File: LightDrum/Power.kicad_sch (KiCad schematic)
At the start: 67 parts, among them U1001 AP3401, U1002 LM22673-SOIC, U701 INA4181 A2, U702 INA4181 A2, U901 74HC2G08

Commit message: Lock REV8 Layout and send to PCB MNF
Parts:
- removed C1021: 100nF, Capacitor_SMD:C_0603_1608Metric, symbol Device:C_Small
- removed U901: 74HC2G08, Package_SO:TSSOP-8_3x3mm_P0.65mm, symbol Daxxn_Logic:74HCT2G08
- renumbered U-XLR-VREF1001 to U1003
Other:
- note removed: "PS LOCKOUT"
- moved on the sheet: C1005, C1022, C1023, C1024, C1025, C1042, C1043, L1002, L1004, R1008, R1009, R1010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

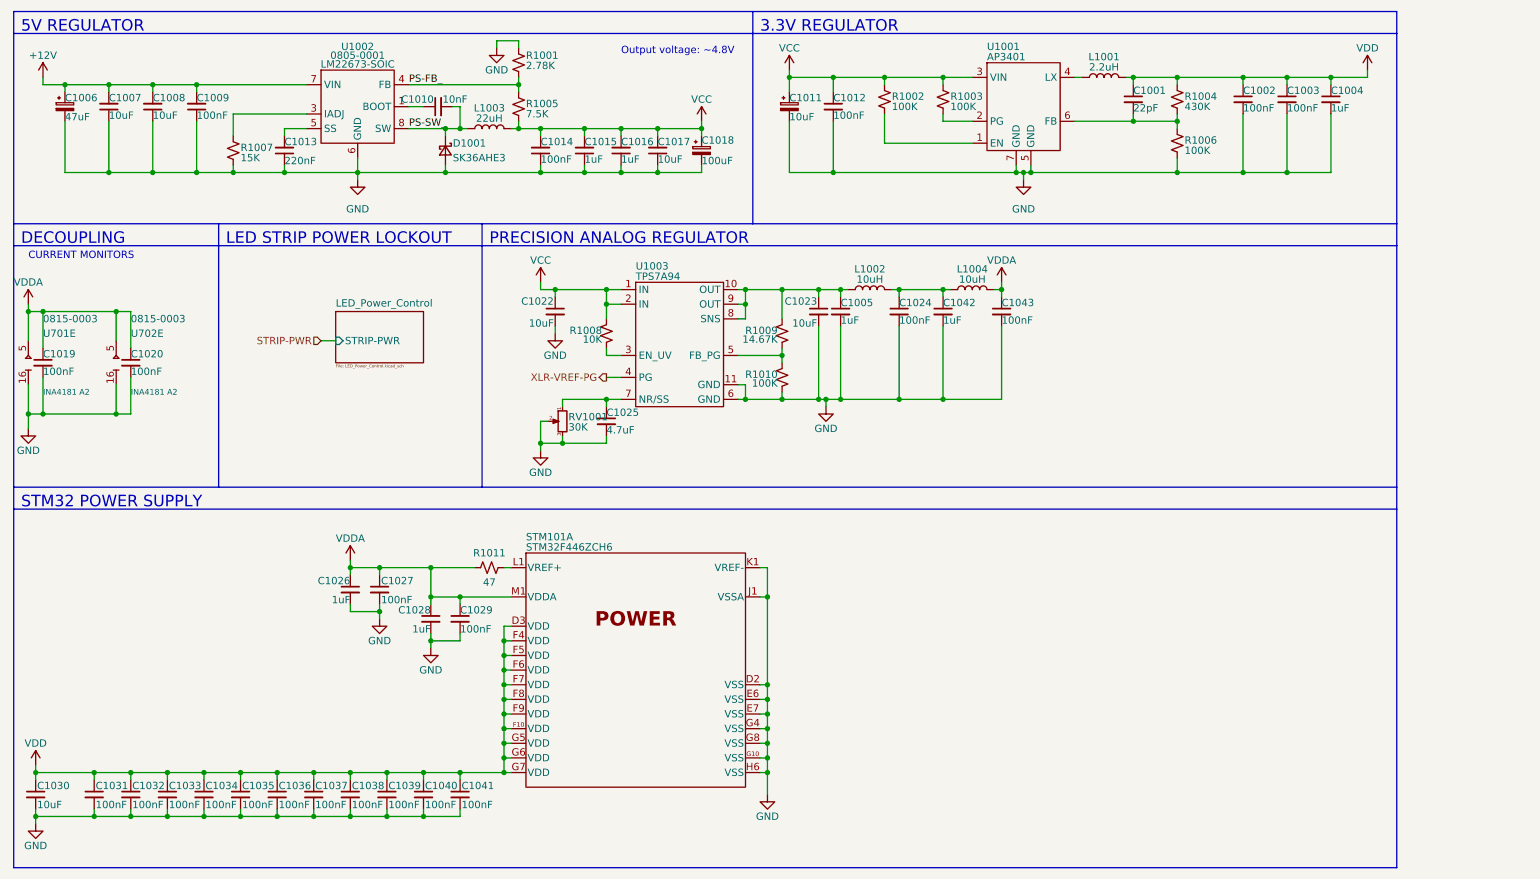
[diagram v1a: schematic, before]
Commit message: Replace old MCU W/ STM32F412
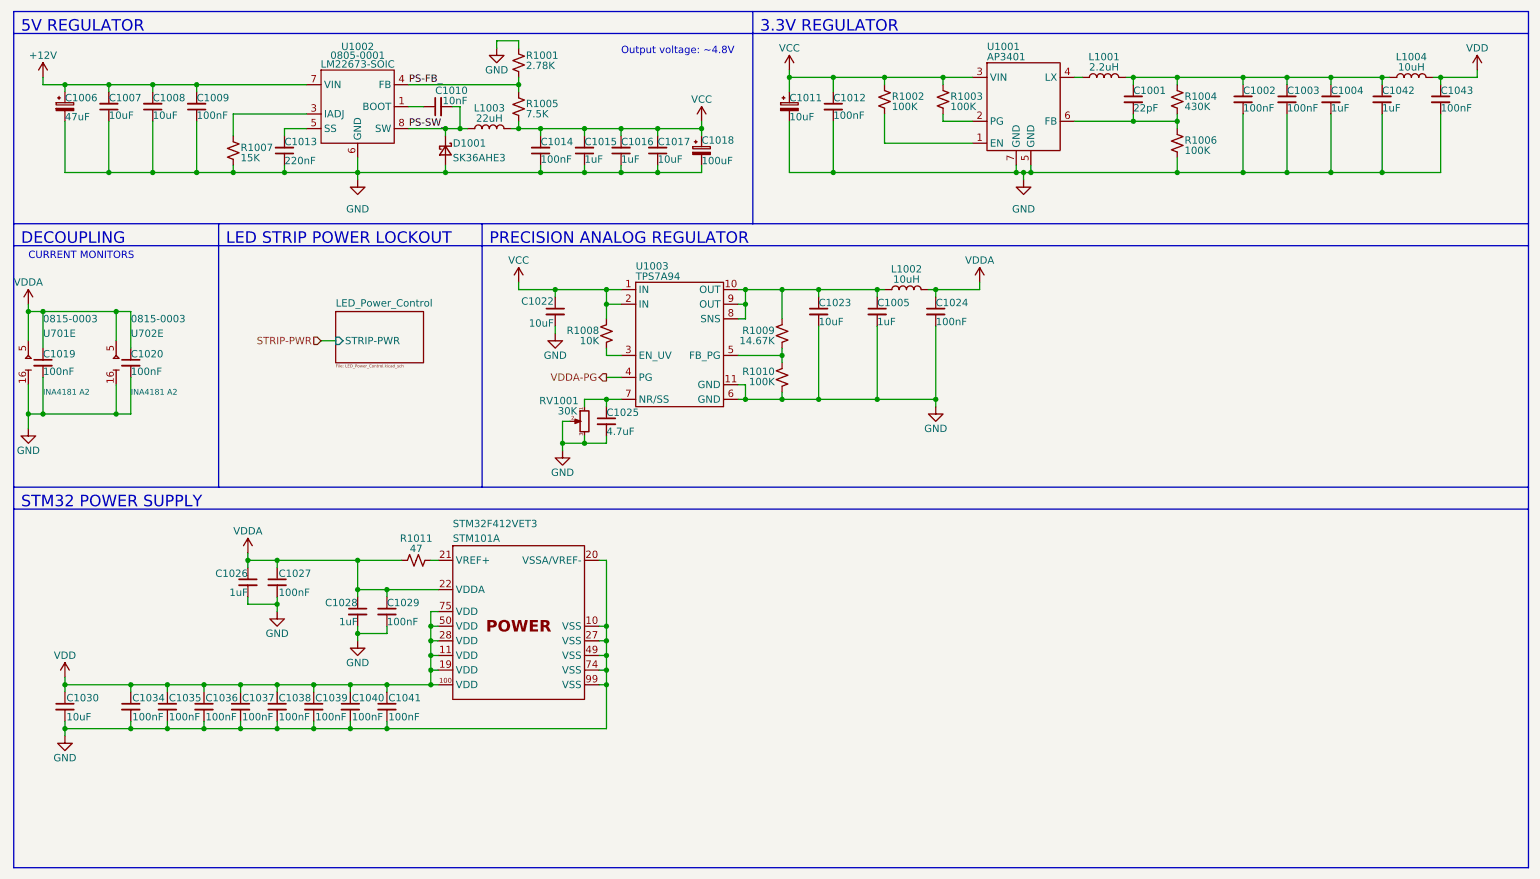
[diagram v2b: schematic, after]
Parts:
- removed C1031, C1032, C1033: 100nF, Capacitor_SMD:C_0402_1005Metric, symbol Device:C_Small
- removed STM101: STM32F446ZCH6, Daxxn_Packages:UFBGA144-7x7xOP6, symbol Daxxn_STMicros:STM32F446ZCH6
- added STM101: STM32F412VET3, Package_QFP:LQFP-100_14x14mm_P0.5mm, symbol Daxxn_STMicros:STM32F412VET3
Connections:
- net GND: now also STM101.10 (VSS), STM101.20 (VSSA/VREF-), STM101.27 (VSS), STM101.49 (VSS), STM101.74 (VSS), STM101.99 (VSS)
- net VDD: now also C1043.1, L1004.2, STM101.100 (VDD), STM101.11 (VDD), STM101.19 (VDD), STM101.28 (VDD), STM101.50 (VDD), STM101.75 (VDD); no longer C1001.1, C1002.1, C1003.1, C1004.1, L1001.2, R1004.1
- net VDDA: now also C1024.1, L1002.2, STM101.22 (VDDA); no longer C1043.1, L1004.2
- net at R1011.1: now also STM101.21 (VREF+)
- net at C1042.1, L1004.1: now also C1001.1, C1002.1, C1003.1, C1004.1, L1001.2, R1004.1; no longer C1024.1, L1002.2
- net XLR-VREF-PG renamed VDDA-PG
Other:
- moved on the sheet: C1005, C1024, C1026, C1027, C1028, C1029, C1030, C1034, C1035, C1036, C1037, C1038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

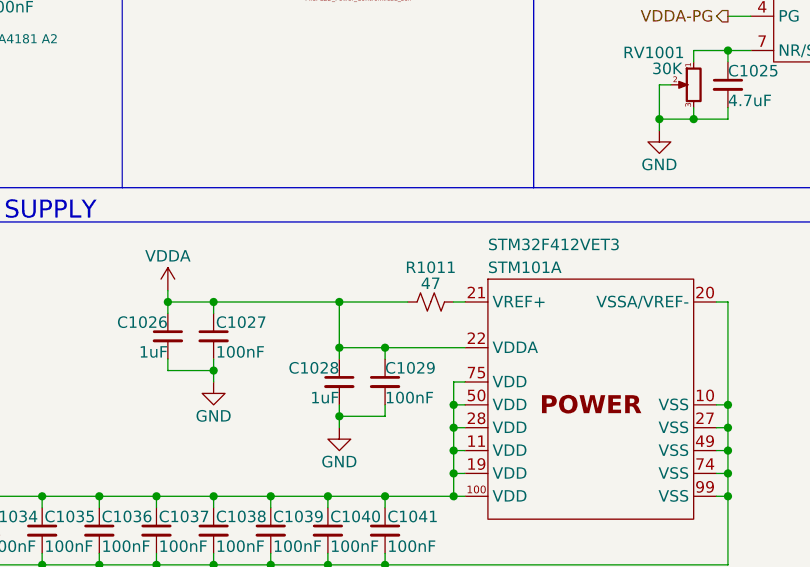
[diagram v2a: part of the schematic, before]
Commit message: Replace MCU finished. REV9
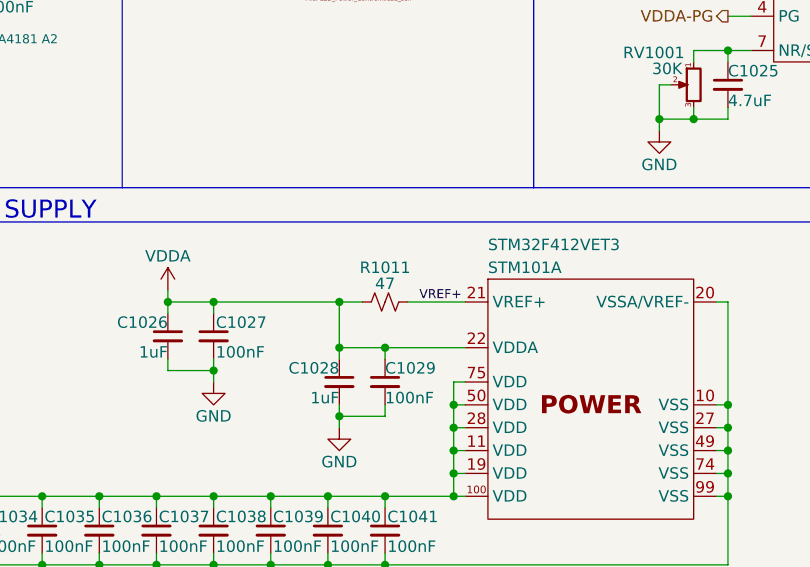
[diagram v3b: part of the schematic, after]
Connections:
- net VREF+: now reaches R1011.1, STM101.21 (VREF+)
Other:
- moved on the sheet: R1011
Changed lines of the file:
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@@
   (title_block
     (title "LightDrum")
-    (rev "REV8")
+    (rev "REV9")
     (company "Daxxn Industries")
   )
@@
     (stroke (width 0) (type default) (color 0 0 0 0))
   )
-  (wire (pts (xy 76.2 111.76) (xy 83.82 111.76))
+  (wire (pts (xy 76.2 111.76) (xy 78.74 111.76))
     (stroke (width 0) (type default) (color 0 0 0 0))
   )
@@
     (stroke (width 0) (type default) (color 0 0 0 0))
   )
-  (wire (pts (xy 88.9 111.76) (xy 90.17 111.76))
+  (wire (pts (xy 83.82 111.76) (xy 90.17 111.76))
     (stroke (width 0) (type default) (color 0 0 0 0))
   )
@@
   (text "DECOUPLING" (at 17.78 57.15 0)
     (effects (font (size 2 2)) (justify left bottom))
+  )
+  (label "VREF+" (at 85.09 111.76 0)
+    (effects (font (size 1 1)) (justify left bottom))
   )
   (label "PS-FB_" (at 85.09 29.21 0)
@@
     (pin "2")
   )
-  (symbol (lib_id "Device:R_Small_US") (at 86.36 111.76 270) (unit 1)
-    (in_bom yes) (on_board yes)
-    (property "Reference" "R1011" (id 0) (at 86.36 107.95 90))
-    (property "Value" "47" (id 1) (at 86.36 109.728 90))
-    (property "Footprint" "Resistor_SMD:R_0402_1005Metric" (id 2) (at 86.36 111.76 0)
-      (effects (font (size 1.27 1.27)) hide)
-    )
-    (property "Datasheet" "~" (id 3) (at 86.36 111.76 0)
+  (symbol (lib_id "Device:R_Small_US") (at 81.28 111.76 270) (unit 1)
+    (in_bom yes) (on_board yes)
+    (property "Reference" "R1011" (id 0) (at 81.28 107.95 90))
+    (property "Value" "47" (id 1) (at 81.28 109.728 90))
+    (property "Footprint" "Resistor_SMD:R_0402_1005Metric" (id 2) (at 81.28 111.76 0)
+      (effects (font (size 1.27 1.27)) hide)
+    )
+    (property "Datasheet" "~" (id 3) (at 81.28 111.76 0)
       (effects (font (size 1.27 1.27)) hide)
     )
@@
     (pin "94")
     (pin "1")
-    (pin "15" (alternate "ADC-10"))
-    (pin "16" (alternate "ADC-11"))
-    (pin "17" (alternate "ADC-12"))
-    (pin "18" (alternate "ADC-13"))
+    (pin "15")
+    (pin "16")
+    (pin "17")
+    (pin "18")
     (pin "2")
     (pin "23" (alternate "TIM2-CH1"))
@@
     (pin "25" (alternate "USART2-TX"))
     (pin "26" (alternate "USART2-RX"))
-    (pin "29")
+    (pin "29" (alternate "ADC-4"))
     (pin "3")
-    (pin "30" (alternate "SPI1-SCK"))
-    (pin "31" (alternate "SPI1-CIPO"))
-    (pin "32" (alternate "SPI1-COPI"))
+    (pin "30" (alternate "ADC-5"))
+    (pin "31" (alternate "ADC-6"))
+    (pin "32" (alternate "ADC-7"))
     (pin "33" (alternate "ADC1-14"))
     (pin "34" (alternate "ADC1-15"))
@@
     (pin "38")
     (pin "39")
-    (pin "4")
+    (pin "4" (alternate "TIM9-CH1"))
     (pin "40")
     (pin "41")
     (pin "42")
-    (pin "43")
-    (pin "44")
-    (pin "45")
+    (pin "43" (alternate "SPI5-SCK"))
+    (pin "44" (alternate "SPI5-CIPO"))
+    (pin "45" (alternate "SPI5-COPI"))
     (pin "46")
     (pin "47" (alternate "SPI2-SCK"))

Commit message: interface layout completed - REV6
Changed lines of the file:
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@@
     (stroke (width 0) (type default) (color 0 0 0 0))
   )
-  (polyline (pts (xy 16.51 165.1) (xy 279.4 165.1))
+  (polyline (pts (xy 16.51 148.59) (xy 279.4 148.59))
     (stroke (width 0) (type default) (color 0 0 0 0))
   )
@@
     (stroke (width 0) (type default) (color 0 0 0 0))
   )
-  (polyline (pts (xy 16.51 102.87) (xy 16.51 165.1))
+  (polyline (pts (xy 16.51 102.87) (xy 16.51 148.59))
     (stroke (width 0) (type default) (color 0 0 0 0))
   )
@@
     (stroke (width 0) (type default) (color 0 0 0 0))
   )
-  (polyline (pts (xy 279.4 165.1) (xy 279.4 102.87))
-    (stroke (width 0) (type default) (color 0 0 0 0))
-  )
+  (polyline (pts (xy 279.4 148.59) (xy 279.4 102.87))
+    (stroke (width 0) (type default) (color 0 0 0 0))
+  )

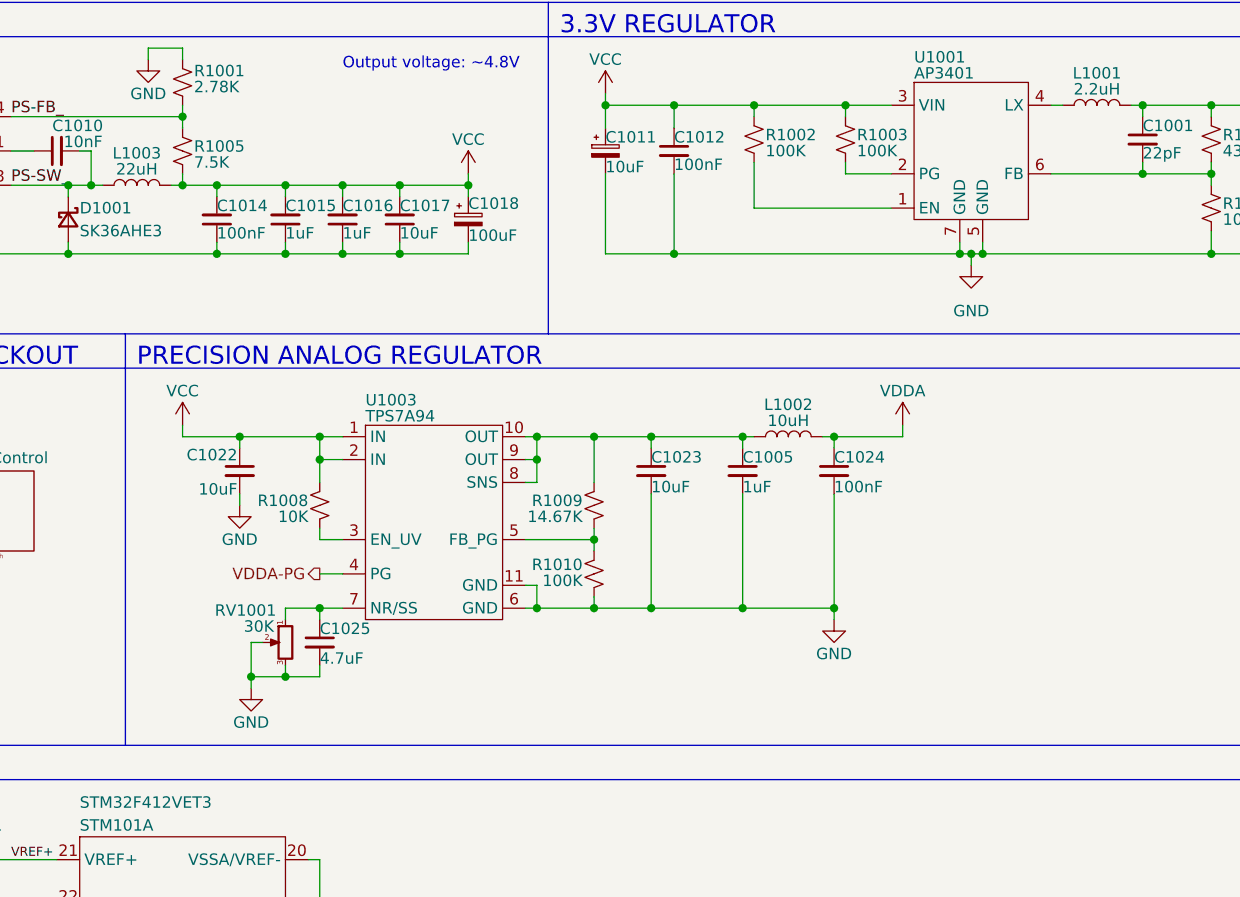
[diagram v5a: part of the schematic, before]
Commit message: Start REV 10 - Fix small issues
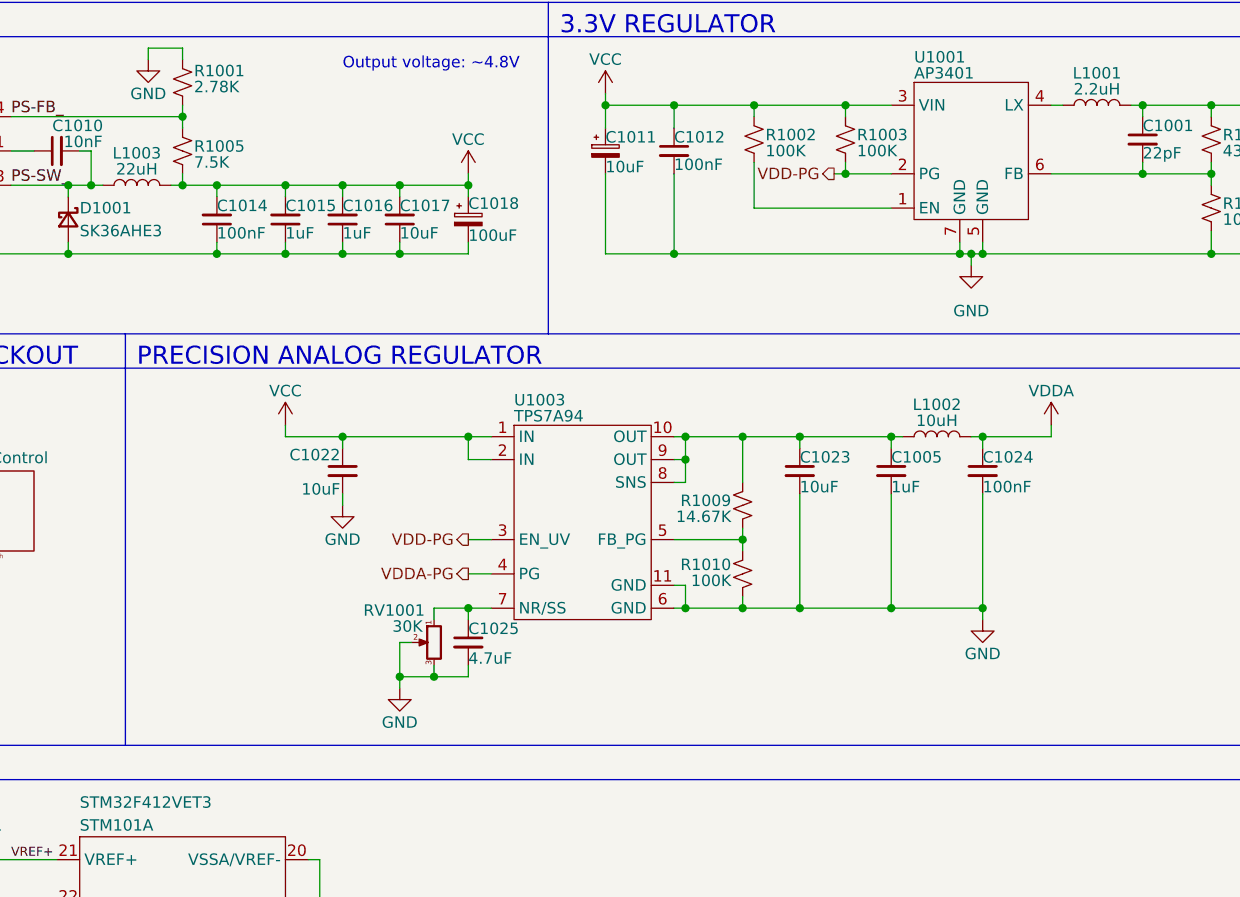
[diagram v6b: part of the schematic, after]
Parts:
- removed R1008: 10K, Resistor_SMD:R_0402_1005Metric, symbol Device:R_Small_US
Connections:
- net VDD-PG: now reaches R1003.2, U1001.2 (PG)
- net VDD-PG: now also U1003.3 (EN_UV)
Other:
- moved on the sheet: C1005, C1022, C1023, C1024, C1025, L1002, R1009, R1010, RV1001, U1003
